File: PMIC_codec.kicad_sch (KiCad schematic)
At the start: 18 parts, among them U5 RK809-2

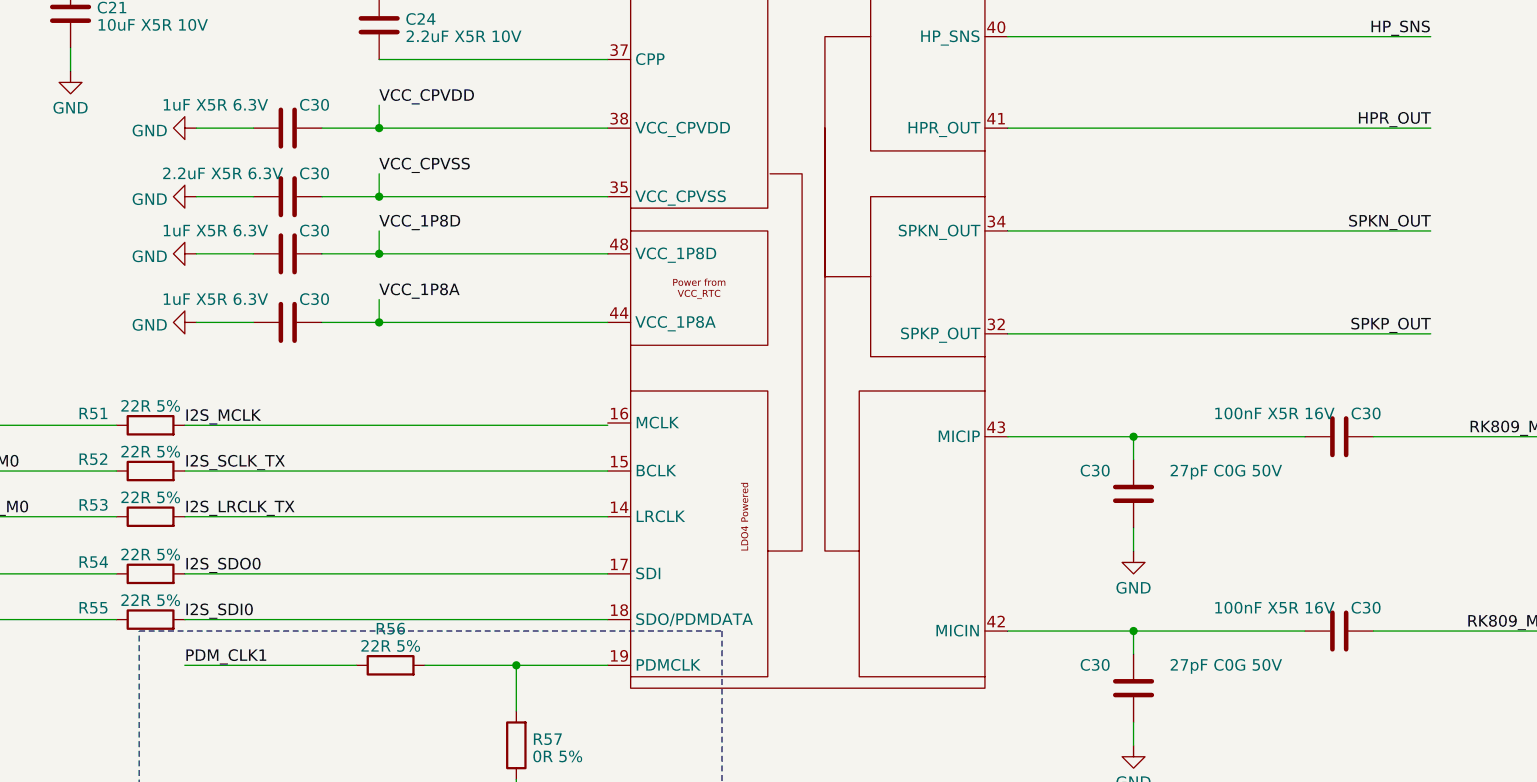
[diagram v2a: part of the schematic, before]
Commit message: updated LCSC selection of capacitors
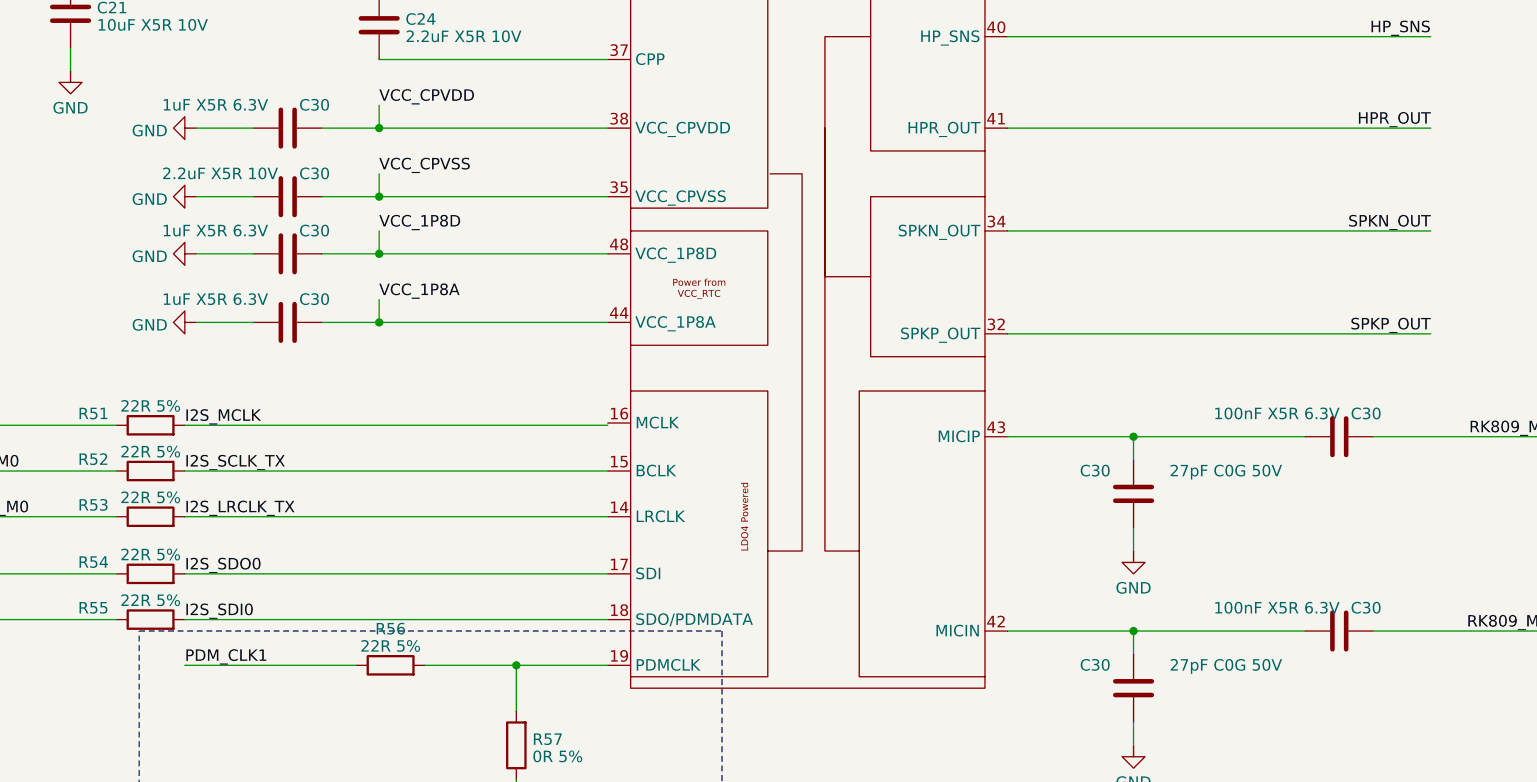
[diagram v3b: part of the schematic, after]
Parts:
- C21: footprint Capacitor_SMD:C_0603_1608Metric -> Capacitor_SMD:C_0402_1005Metric; LCSC C469532 -> C77000; Model GRM188B31A106KE69D -> GRM155R61A106ME44D
- C24: Model (none) -> GRM155R61A225KE01D; Vendor (none) -> muRata(村田)
- C30: value 100nF X5R 16V -> 100nF X5R 6.3V; footprint Capacitor_SMD:C_0402_1005Metric -> Capacitor_SMD:C_0201_0603Metric; LCSC (none) -> C76934; Model (none) -> GRM033R61A104KE15D; Vendor (none) -> muRata(村田)
- C30: footprint Capacitor_SMD:C_0402_1005Metric -> Capacitor_SMD:C_0201_0603Metric; LCSC (none) -> C384976; Model (none) -> GRM0335C1H270GA01D; Vendor (none) -> muRata(村田)
- C30: value 2.2uF X5R 6.3V -> 2.2uF X5R 10V; Model (none) -> GRM155R61A225KE01D; Vendor (none) -> muRata(村田)
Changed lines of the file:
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@@
       (effects (font (size 1.27 1.27)) (justify left))
     )
-    (property "Value" "100nF X5R 16V" (at 222.25 115.57 90)
-      (effects (font (size 1.27 1.27)) (justify left))
-    )
-    (property "Footprint" "Capacitor_SMD:C_0402_1005Metric" (at 232.41 117.1448 0)
+    (property "Value" "100nF X5R 6.3V" (at 222.25 115.57 90)
+      (effects (font (size 1.27 1.27)) (justify left))
+    )
+    (property "Footprint" "Capacitor_SMD:C_0201_0603Metric" (at 232.41 117.1448 0)
       (effects (font (size 1.27 1.27)) hide)
     )
@@
       (effects (font (size 1.27 1.27)) hide)
     )
+    (property "Description" "容值: 100nF 精度: ±10% 额定电压: 10V 材质(温度系数): X5R 材质:X5R" (at 236.22 118.11 0)
+      (effects (font (size 1.27 1.27)) hide)
+    )
+    (property "Model" "GRM033R61A104KE15D" (at 236.22 118.11 0)
+      (effects (font (size 1.27 1.27)) hide)
+    )
+    (property "Vendor" "muRata(村田)" (at 236.22 118.11 0)
+      (effects (font (size 1.27 1.27)) hide)
+    )
+    (property "LCSC" "C76934" (at 236.22 118.11 0)
+      (effects (font (size 1.27 1.27)) hide)
+    )
     (pin "1")
     (pin "2")
@@
       (effects (font (size 1.27 1.27)) (justify left))
     )
-    (property "Footprint" "Capacitor_SMD:C_0402_1005Metric" (at 212.3948 128.27 0)
+    (property "Footprint" "Capacitor_SMD:C_0201_0603Metric" (at 212.3948 128.27 0)
       (effects (font (size 1.27 1.27)) hide)
     )
     (property "Datasheet" "~" (at 213.36 124.46 0)
+      (effects (font (size 1.27 1.27)) hide)
+    )
+    (property "Description" "容值: 27pF 精度: ±2% 额定电压: 50V 材质(温度系数): C0G 材质:C0G" (at 213.36 124.46 0)
+      (effects (font (size 1.27 1.27)) hide)
+    )
+    (property "LCSC" "C384976" (at 213.36 124.46 0)
+      (effects (font (size 1.27 1.27)) hide)
+    )
+    (property "Model" "GRM0335C1H270GA01D" (at 213.36 124.46 0)
+      (effects (font (size 1.27 1.27)) hide)
+    )
+    (property "Vendor" "muRata(村田)" (at 213.36 124.46 0)
       (effects (font (size 1.27 1.27)) hide)
     )
@@
       (effects (font (size 1.27 1.27)) (justify left))
     )
-    (property "Value" "100nF X5R 16V" (at 222.25 93.98 90)
-      (effects (font (size 1.27 1.27)) (justify left))
-    )
-    (property "Footprint" "Capacitor_SMD:C_0402_1005Metric" (at 232.41 95.5548 0)
+    (property "Value" "100nF X5R 6.3V" (at 222.25 93.98 90)
+      (effects (font (size 1.27 1.27)) (justify left))
+    )
+    (property "Footprint" "Capacitor_SMD:C_0201_0603Metric" (at 232.41 95.5548 0)
       (effects (font (size 1.27 1.27)) hide)
     )
@@
       (effects (font (size 1.27 1.27)) hide)
     )
+    (property "Description" "容值: 100nF 精度: ±10% 额定电压: 10V 材质(温度系数): X5R 材质:X5R" (at 236.22 96.52 0)
+      (effects (font (size 1.27 1.27)) hide)
+    )
+    (property "Model" "GRM033R61A104KE15D" (at 236.22 96.52 0)
+      (effects (font (size 1.27 1.27)) hide)
+    )
+    (property "Vendor" "muRata(村田)" (at 236.22 96.52 0)
+      (effects (font (size 1.27 1.27)) hide)
+    )
+    (property "LCSC" "C76934" (at 236.22 96.52 0)
+      (effects (font (size 1.27 1.27)) hide)
+    )
     (pin "1")
     (pin "2")
@@
       (effects (font (size 1.27 1.27)) (justify left))
     )
-    (property "Footprint" "Capacitor_SMD:C_0603_1608Metric" (at 96.2152 53.34 0)
+    (property "Footprint" "Capacitor_SMD:C_0402_1005Metric" (at 96.2152 53.34 0)
       (effects (font (size 1.27 1.27)) hide)
     )
@@
       (effects (font (size 1.27 1.27)) hide)
     )
-    (property "Description" "容值: 10uF 精度: ±10% 额定电压: 10V 材质(温度系数): B B(JIS)" (at 95.25 49.53 0)
-      (effects (font (size 1.27 1.27)) hide)
-    )
-    (property "LCSC" "C469532" (at 95.25 49.53 0)
-      (effects (font (size 1.27 1.27)) hide)
-    )
-    (property "Model" "GRM188B31A106KE69D" (at 95.25 49.53 0)
+    (property "Description" "容值: 10uF 精度: ±20% 额定电压: 10V 材质(温度系数): X5R 材质:X5R" (at 95.25 49.53 0)
+      (effects (font (size 1.27 1.27)) hide)
+    )
+    (property "LCSC" "C77000" (at 95.25 49.53 0)
+      (effects (font (size 1.27 1.27)) hide)
+    )
+    (property "Model" "GRM155R61A106ME44D" (at 95.25 49.53 0)
       (effects (font (size 1.27 1.27)) hide)
     )
@@
     )
     (property "Datasheet" "~" (at 129.54 50.8 0)
+      (effects (font (size 1.27 1.27)) hide)
+    )
+    (property "Description" "容值: 2.2uF 精度: ±10% 额定电压: 10V 材质(温度系数): X5R" (at 129.54 50.8 0)
+      (effects (font (size 1.27 1.27)) hide)
+    )
+    (property "Model" "GRM155R61A225KE01D" (at 129.54 50.8 0)
+      (effects (font (size 1.27 1.27)) hide)
+    )
+    (property "Vendor" "muRata(村田)" (at 129.54 50.8 0)
       (effects (font (size 1.27 1.27)) hide)
     )
@@
       (effects (font (size 1.27 1.27)) (justify left))
     )
-    (property "Footprint" "Capacitor_SMD:C_0402_1005Metric" (at 212.3948 106.68 0)
+    (property "Footprint" "Capacitor_SMD:C_0201_0603Metric" (at 212.3948 106.68 0)
       (effects (font (size 1.27 1.27)) hide)
     )
@@
       (effects (font (size 1.27 1.27)) hide)
     )
+    (property "Description" "容值: 27pF 精度: ±2% 额定电压: 50V 材质(温度系数): C0G 材质:C0G" (at 213.36 102.87 0)
+      (effects (font (size 1.27 1.27)) hide)
+    )
+    (property "LCSC" "C384976" (at 213.36 102.87 0)
+      (effects (font (size 1.27 1.27)) hide)
+    )
+    (property "Model" "GRM0335C1H270GA01D" (at 213.36 102.87 0)
+      (effects (font (size 1.27 1.27)) hide)
+    )
+    (property "Vendor" "muRata(村田)" (at 213.36 102.87 0)
+      (effects (font (size 1.27 1.27)) hide)
+    )
     (pin "1")
     (pin "2")
@@
       (effects (font (size 1.27 1.27)) (justify left))
     )
-    (property "Value" "2.2uF X5R 6.3V" (at 105.41 67.31 90)
+    (property "Value" "2.2uF X5R 10V" (at 105.41 67.31 90)
       (effects (font (size 1.27 1.27)) (justify left))
     )
@@
       (effects (font (size 1.27 1.27)) hide)
     )
+    (property "Description" "容值: 2.2uF 精度: ±10% 额定电压: 10V 材质(温度系数): X5R" (at 119.38 69.85 0)
+      (effects (font (size 1.27 1.27)) hide)
+    )
+    (property "Model" "GRM155R61A225KE01D" (at 119.38 69.85 0)
+      (effects (font (size 1.27 1.27)) hide)
+    )
+    (property "Vendor" "muRata(村田)" (at 119.38 69.85 0)
+      (effects (font (size 1.27 1.27)) hide)
+    )

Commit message: layout SoC Power and DDR capacitors
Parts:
- C30: LCSC C76934 -> C76928; Model GRM033R61A104KE15D -> GRM033R60J104KE19D
- C30: footprint Capacitor_SMD:C_0201_0603Metric -> Capacitor_SMD:C_0402_1005Metric; LCSC C76929 -> C15684; Model GRM033R60J105KEA2D -> GRM155R60J105KE19D
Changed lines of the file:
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@@
       (effects (font (size 1.27 1.27)) hide)
     )
-    (property "Description" "容值: 100nF 精度: ±10% 额定电压: 10V 材质(温度系数): X5R 材质:X5R" (at 236.22 118.11 0)
-      (effects (font (size 1.27 1.27)) hide)
-    )
-    (property "Model" "GRM033R61A104KE15D" (at 236.22 118.11 0)
+    (property "Description" "容值: 100nF 精度: ±10% 额定电压: 6.3V 材质(温度系数): X5R 材质:X5R" (at 236.22 118.11 0)
+      (effects (font (size 1.27 1.27)) hide)
+    )
+    (property "Model" "GRM033R60J104KE19D" (at 236.22 118.11 0)
       (effects (font (size 1.27 1.27)) hide)
     )
@@
       (effects (font (size 1.27 1.27)) hide)
     )
-    (property "LCSC" "C76934" (at 236.22 118.11 0)
+    (property "LCSC" "C76928" (at 236.22 118.11 0)
       (effects (font (size 1.27 1.27)) hide)
     )
@@
       (effects (font (size 1.27 1.27)) (justify left))
     )
-    (property "Footprint" "Capacitor_SMD:C_0201_0603Metric" (at 115.57 75.2348 0)
+    (property "Footprint" "Capacitor_SMD:C_0402_1005Metric" (at 115.57 75.2348 0)
       (effects (font (size 1.27 1.27)) hide)
     )
@@
       (effects (font (size 1.27 1.27)) hide)
     )
-    (property "LCSC" "C76929" (at 119.38 76.2 0)
-      (effects (font (size 1.27 1.27)) hide)
-    )
-    (property "Model" "GRM033R60J105KEA2D" (at 119.38 76.2 0)
+    (property "LCSC" "C15684" (at 119.38 76.2 0)
+      (effects (font (size 1.27 1.27)) hide)
+    )
+    (property "Model" "GRM155R60J105KE19D" (at 119.38 76.2 0)
       (effects (font (size 1.27 1.27)) hide)
     )
@@
       (effects (font (size 1.27 1.27)) hide)
     )
-    (property "Description" "容值: 100nF 精度: ±10% 额定电压: 10V 材质(温度系数): X5R 材质:X5R" (at 236.22 96.52 0)
-      (effects (font (size 1.27 1.27)) hide)
-    )
-    (property "Model" "GRM033R61A104KE15D" (at 236.22 96.52 0)
+    (property "Description" "容值: 100nF 精度: ±10% 额定电压: 6.3V 材质(温度系数): X5R 材质:X5R" (at 236.22 96.52 0)
+      (effects (font (size 1.27 1.27)) hide)
+    )
+    (property "Model" "GRM033R60J104KE19D" (at 236.22 96.52 0)
       (effects (font (size 1.27 1.27)) hide)
     )
@@
       (effects (font (size 1.27 1.27)) hide)
     )
-    (property "LCSC" "C76934" (at 236.22 96.52 0)
+    (property "LCSC" "C76928" (at 236.22 96.52 0)
       (effects (font (size 1.27 1.27)) hide)
     )
@@
       (effects (font (size 1.27 1.27)) (justify left))
     )
-    (property "Footprint" "Capacitor_SMD:C_0201_0603Metric" (at 115.57 61.2648 0)
+    (property "Footprint" "Capacitor_SMD:C_0402_1005Metric" (at 115.57 61.2648 0)
       (effects (font (size 1.27 1.27)) hide)
     )
@@
       (effects (font (size 1.27 1.27)) hide)
     )
-    (property "LCSC" "C76929" (at 119.38 62.23 0)
-      (effects (font (size 1.27 1.27)) hide)
-    )
-    (property "Model" "GRM033R60J105KEA2D" (at 119.38 62.23 0)
+    (property "LCSC" "C15684" (at 119.38 62.23 0)
+      (effects (font (size 1.27 1.27)) hide)
+    )
+    (property "Model" "GRM155R60J105KE19D" (at 119.38 62.23 0)
       (effects (font (size 1.27 1.27)) hide)
     )
@@
       (effects (font (size 1.27 1.27)) (justify left))
     )
-    (property "Footprint" "Capacitor_SMD:C_0201_0603Metric" (at 115.57 82.8548 0)
+    (property "Footprint" "Capacitor_SMD:C_0402_1005Metric" (at 115.57 82.8548 0)
       (effects (font (size 1.27 1.27)) hide)
     )
@@
       (effects (font (size 1.27 1.27)) hide)
     )
-    (property "LCSC" "C76929" (at 119.38 83.82 0)
-      (effects (font (size 1.27 1.27)) hide)
-    )
-    (property "Model" "GRM033R60J105KEA2D" (at 119.38 83.82 0)
-      (effects (font (size 1.27 1.27)) hide)
-    )
+    (property "LCSC" "C15684" (at 119.38 83.82 0)
+      (effects (font (size 1.27 1.27)) hide)
+    )
+    (property "Model" "GRM155R60J105KE19D" (at 119.38 83.82 0)
+      (effects (font (size 1.27 1.27)) hide)
+    )

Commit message: updated Resistors
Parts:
- R51, R52, R53, R54, R55, R56: LCSC (none) -> C59651; Model (none) -> 0402WGF221JTCE; Vendor (none) -> UNI-ROYAL(厚声)
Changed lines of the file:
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@@
+      (effects (font (size 1.27 1.27)) hide)
+    )
+    (property "Description" "电阻类型: 厚膜电阻 阻值: 22.1Ω 精度: ±1% 功率: 1/16W 温度系数: ±100ppm/℃ 最大工作电压: 50V 工作温度" (at 104.14 111.76 0)
+      (effects (font (size 1.27 1.27)) hide)
+    )
+    (property "LCSC" "C59651" (at 104.14 111.76 0)
+      (effects (font (size 1.27 1.27)) hide)
+    )
+    (property "Model" "0402WGF221JTCE" (at 104.14 111.76 0)
+      (effects (font (size 1.27 1.27)) hide)
+    )
+    (property "Vendor" "UNI-ROYAL(厚声)" (at 104.14 111.76 0)
       (effects (font (size 1.27 1.27)) hide)
     )
@@
     )
     (property "Datasheet" "~" (at 130.81 121.92 0)
+      (effects (font (size 1.27 1.27)) hide)
+    )
+    (property "Description" "电阻类型: 厚膜电阻 阻值: 22.1Ω 精度: ±1% 功率: 1/16W 温度系数: ±100ppm/℃ 最大工作电压: 50V 工作温度" (at 130.81 121.92 0)
+      (effects (font (size 1.27 1.27)) hide)
+    )
+    (property "LCSC" "C59651" (at 130.81 121.92 0)
+      (effects (font (size 1.27 1.27)) hide)
+    )
+    (property "Model" "0402WGF221JTCE" (at 130.81 121.92 0)
+      (effects (font (size 1.27 1.27)) hide)
+    )
+    (property "Vendor" "UNI-ROYAL(厚声)" (at 130.81 121.92 0)
       (effects (font (size 1.27 1.27)) hide)
     )
@@
       (effects (font (size 1.27 1.27)) hide)
     )
+    (property "Description" "电阻类型: 厚膜电阻 阻值: 22.1Ω 精度: ±1% 功率: 1/16W 温度系数: ±100ppm/℃ 最大工作电压: 50V 工作温度" (at 104.14 95.25 0)
+      (effects (font (size 1.27 1.27)) hide)
+    )
+    (property "LCSC" "C59651" (at 104.14 95.25 0)
+      (effects (font (size 1.27 1.27)) hide)
+    )
+    (property "Model" "0402WGF221JTCE" (at 104.14 95.25 0)
+      (effects (font (size 1.27 1.27)) hide)
+    )
+    (property "Vendor" "UNI-ROYAL(厚声)" (at 104.14 95.25 0)
+      (effects (font (size 1.27 1.27)) hide)
+    )
     (pin "1")
     (pin "2")
@@
       (effects (font (size 1.27 1.27)) hide)
     )
+    (property "Description" "电阻类型: 厚膜电阻 阻值: 22.1Ω 精度: ±1% 功率: 1/16W 温度系数: ±100ppm/℃ 最大工作电压: 50V 工作温度" (at 104.14 100.33 0)
+      (effects (font (size 1.27 1.27)) hide)
+    )
+    (property "LCSC" "C59651" (at 104.14 100.33 0)
+      (effects (font (size 1.27 1.27)) hide)
+    )
+    (property "Model" "0402WGF221JTCE" (at 104.14 100.33 0)
+      (effects (font (size 1.27 1.27)) hide)
+    )
+    (property "Vendor" "UNI-ROYAL(厚声)" (at 104.14 100.33 0)
+      (effects (font (size 1.27 1.27)) hide)
+    )
     (pin "1")
     (pin "2")
@@
       (effects (font (size 1.27 1.27)) hide)
     )
+    (property "Description" "电阻类型: 厚膜电阻 阻值: 22.1Ω 精度: ±1% 功率: 1/16W 温度系数: ±100ppm/℃ 最大工作电压: 50V 工作温度" (at 104.14 105.41 0)
+      (effects (font (size 1.27 1.27)) hide)
+    )
+    (property "LCSC" "C59651" (at 104.14 105.41 0)
+      (effects (font (size 1.27 1.27)) hide)
+    )
+    (property "Model" "0402WGF221JTCE" (at 104.14 105.41 0)
+      (effects (font (size 1.27 1.27)) hide)
+    )
+    (property "Vendor" "UNI-ROYAL(厚声)" (at 104.14 105.41 0)
+      (effects (font (size 1.27 1.27)) hide)
+    )
     (pin "1")
     (pin "2")
@@
       (effects (font (size 1.27 1.27)) hide)
     )
+    (property "Description" "电阻类型: 厚膜电阻 阻值: 22.1Ω 精度: ±1% 功率: 1/16W 温度系数: ±100ppm/℃ 最大工作电压: 50V 工作温度" (at 104.14 116.84 0)
+      (effects (font (size 1.27 1.27)) hide)
+    )
+    (property "LCSC" "C59651" (at 104.14 116.84 0)
+      (effects (font (size 1.27 1.27)) hide)
+    )
+    (property "Model" "0402WGF221JTCE" (at 104.14 116.84 0)
+      (effects (font (size 1.27 1.27)) hide)
+    )
+    (property "Vendor" "UNI-ROYAL(厚声)" (at 104.14 116.84 0)
+      (effects (font (size 1.27 1.27)) hide)
+    )
